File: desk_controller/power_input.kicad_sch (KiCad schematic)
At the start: 1 part

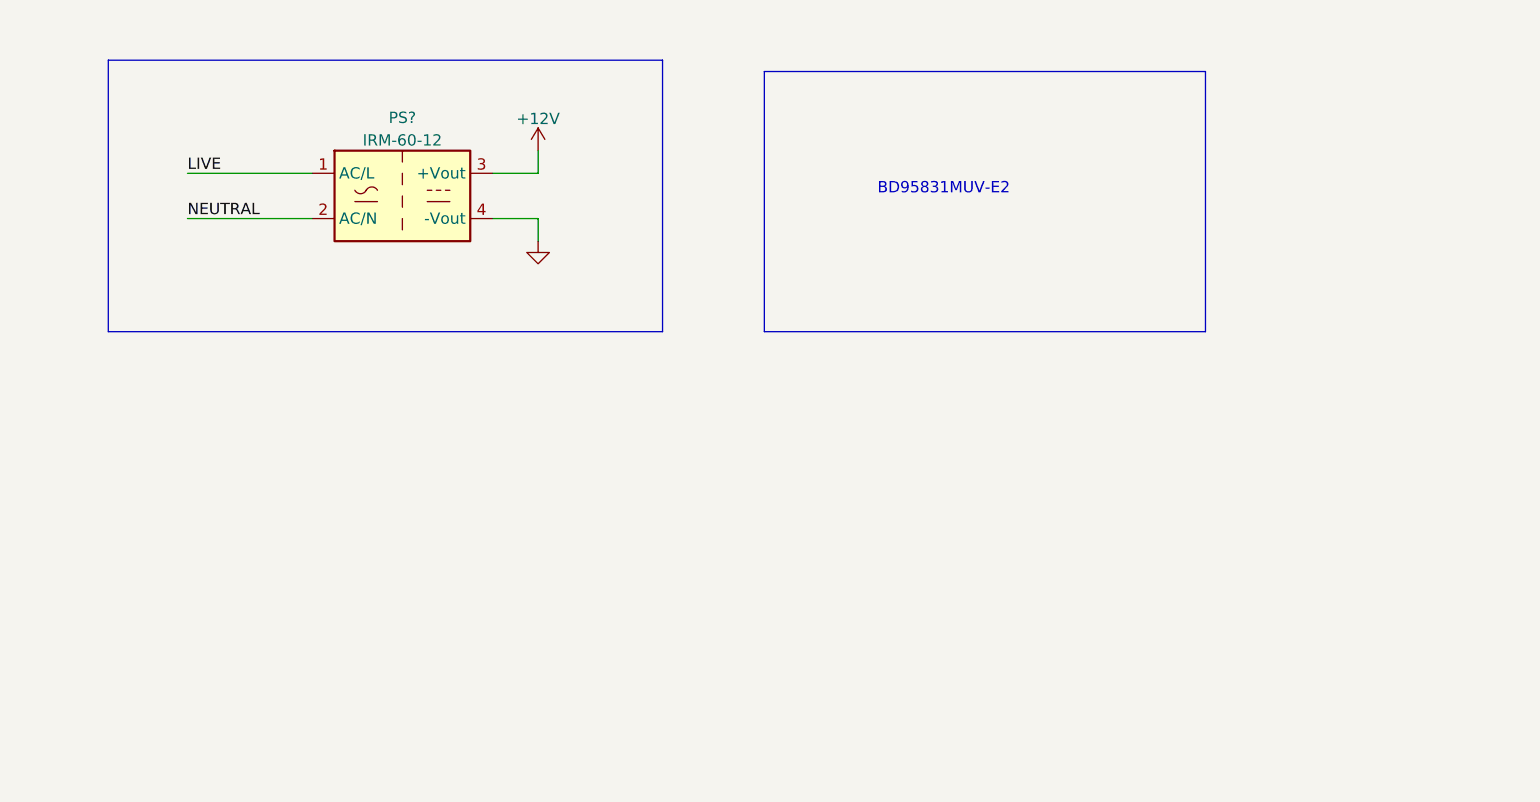
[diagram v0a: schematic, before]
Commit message: Buck converter sch, rs232 transceiver
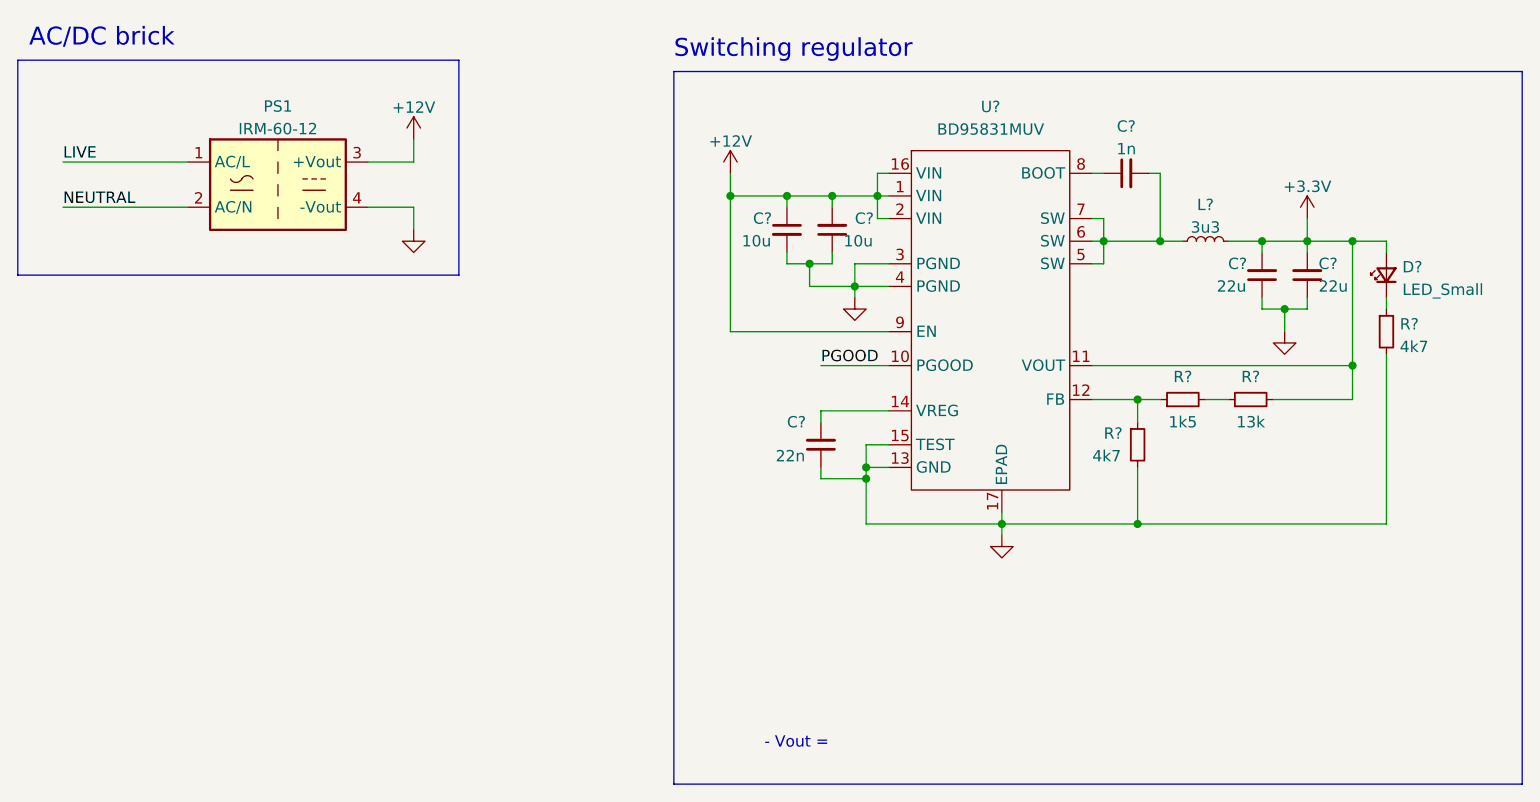
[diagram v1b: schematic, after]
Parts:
- added C? (x2): 22u, symbol Device:C_Small
- added C?: 22n, symbol Device:C_Small
- added C? (x2): 10u, symbol Device:C_Small
- added C?: 1n, symbol Device:C_Small
- added D?: LED_Small, symbol Device:LED_Small
- added L?: 3u3, symbol Device:L_Small
- added R? (x2): 4k7, symbol Device:R_Small
- added R?: 13k, symbol Device:R_Small
- added R?: 1k5, symbol Device:R_Small
- added U?: BD95831MUV, symbol BD95831MUV:BD95831MUV
- gave numbers to parts that had none: 1
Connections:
- net +12V: now also C?.1, C?.2, U?.1 (VIN), U?.16 (VIN), U?.2 (VIN), U?.9 (EN)
- net GND: now also C?.1, C?.1, C?.1, C?.1, C?.2, R?.2, R?.2, U?.13 (GND), U?.15 (TEST), U?.17 (EPAD), U?.3 (PGND), U?.4 (PGND)
- new net: R?.1, R?.1, U?.12 (FB)
- new net: C?.2, U?.14 (VREG)
- new net: C?.2, L?.1, U?.5 (SW), U?.6 (SW), U?.7 (SW)
- new net: C?.1, U?.8 (BOOT)
- new net: D?.1 (K), R?.1
- new net: R?.1, R?.2
- new net +3.3V: C?.2, C?.2, D?.2 (A), L?.2, R?.2, U?.11 (VOUT)
- new net PGOOD: U?.10 (PGOOD)
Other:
- note added: "- Vout ="
- note added: "AC/DC brick"
- note added: "Switching regulator"
- note removed: "BD95831MUV-E2"
- moved on the sheet: PS1

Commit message: Sch fixes, initial board layout
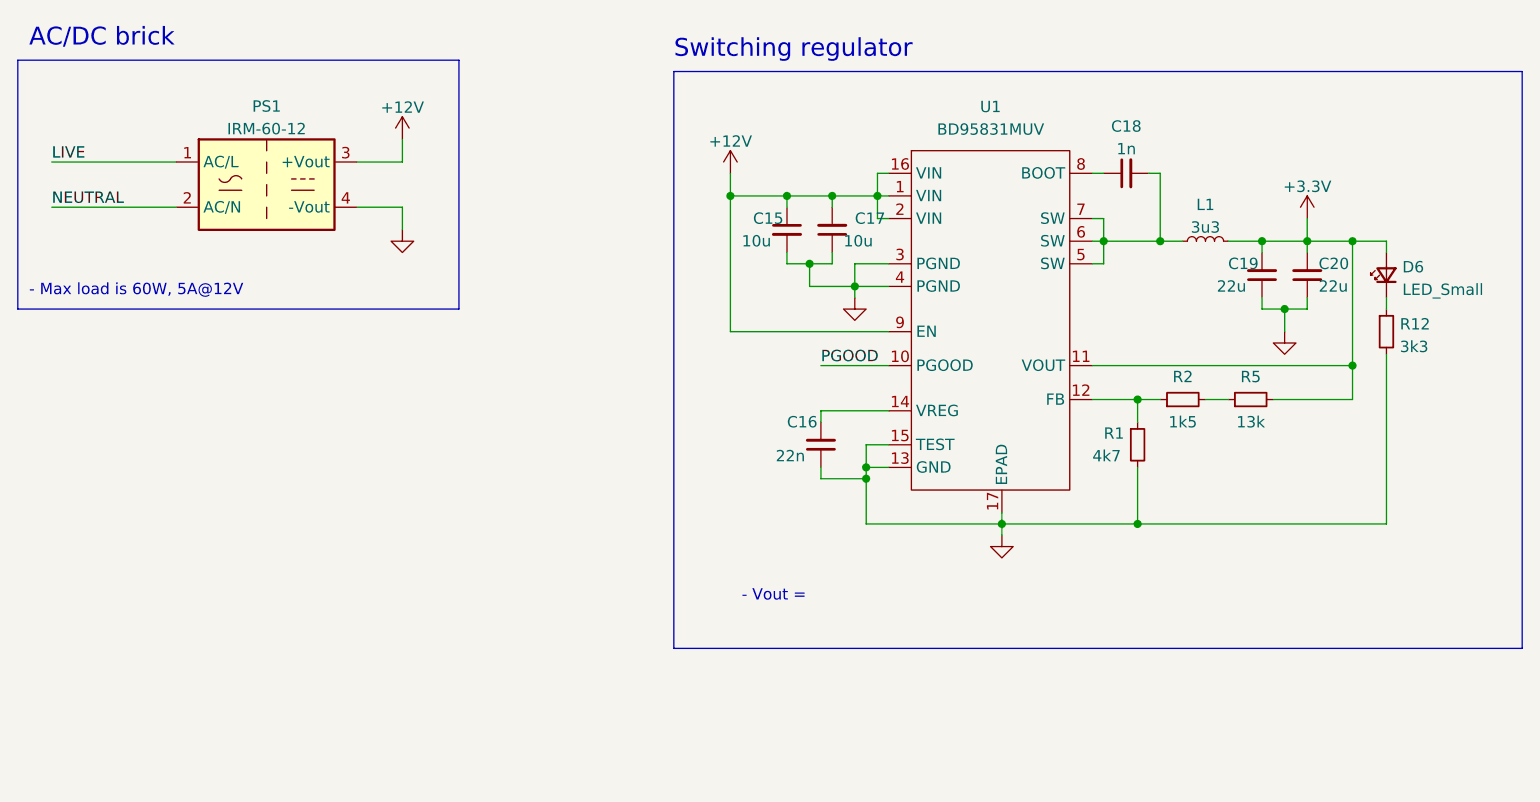
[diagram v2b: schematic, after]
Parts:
- C15, C16, C17, C18, C19, C20: renamed from C?; footprint (none) -> Capacitor_SMD:C_0603_1608Metric
- R1, R2, R5: renamed from R?; footprint (none) -> Resistor_SMD:R_0603_1608Metric
- R12: renamed from R?; value 4k7 -> 3k3; footprint (none) -> Resistor_SMD:R_0603_1608Metric
- U1: renamed from U?; footprint (none) -> Potentiometer_THT:Potentiometer_Bourns_3386F_Vertical
- gave numbers to parts that had none: 2
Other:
- note added: "- Max load is 60W, 5A@12V"
- moved on the sheet: PS1

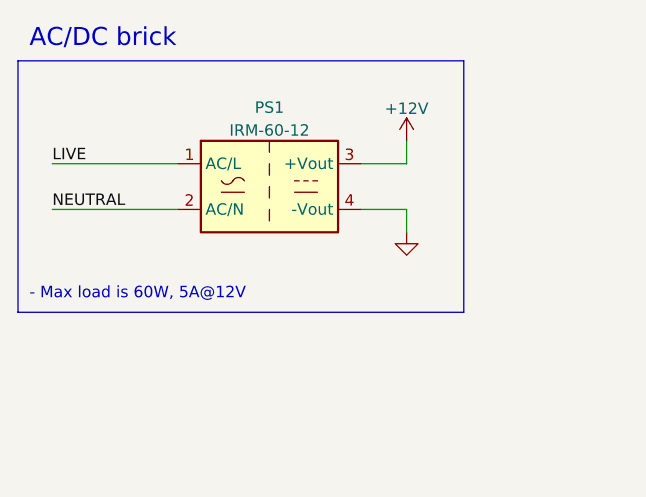
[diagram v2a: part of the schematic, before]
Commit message: Removed acdc brick
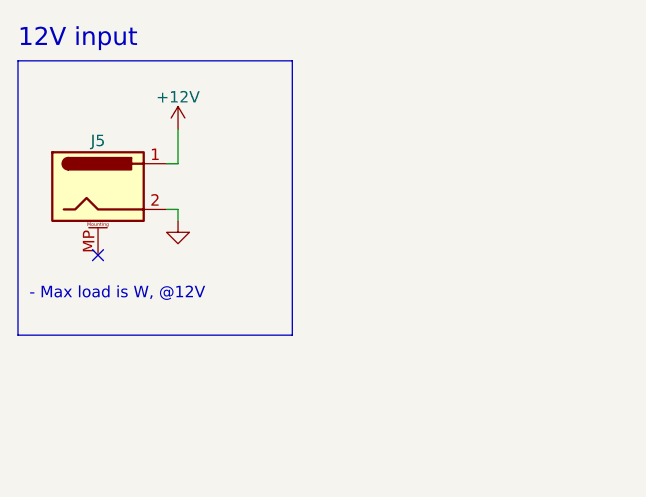
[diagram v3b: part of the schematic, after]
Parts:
- removed PS1: IRM-60-12, Converter_ACDC:Converter_ACDC_MeanWell_IRM-60-xx_THT, symbol Converter_ACDC:IRM-60-12
- added J5: Barrel_Jack_MountingPin, Connector_BarrelJack:BarrelJack_GCT_DCJ200-10-A_Horizontal, symbol Connector:Barrel_Jack_MountingPin
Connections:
- net +12V: now also J5.1
- net GND: now also J5.2
- no-connect marks 0 -> 1
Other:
- note added: "- Max load is W, @12V"
- note added: "12V input"
- note removed: "- Max load is 60W, 5A@12V"
- note removed: "AC/DC brick"
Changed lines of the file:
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@@
   (junction (at 162.56 68.58) (diameter 0) (color 0 0 0 0)
   )
+  (no_connect (at 74.93 74.93))
   (wire (pts (xy 201.93 73.66) (xy 205.74 73.66))
     (stroke (width 0) (type default) (color 0 0 0 0))
@@
     (stroke (width 0) (type default) (color 0 0 0 0))
   )
-  (polyline (pts (xy 66.04 53.34) (xy 115.57 53.34))
+  (polyline (pts (xy 66.04 53.34) (xy 96.52 53.34))
     (stroke (width 0) (type default) (color 0 0 0 0))
   )
@@
     (stroke (width 0) (type default) (color 0 0 0 0))
   )
+  (wire (pts (xy 83.82 60.96) (xy 83.82 64.77))
+    (stroke (width 0) (type default) (color 0 0 0 0))
+  )
   (wire (pts (xy 162.56 66.04) (xy 162.56 68.58))
     (stroke (width 0) (type default) (color 0 0 0 0))
@@
     (stroke (width 0) (type default) (color 0 0 0 0))
   )
-  (polyline (pts (xy 66.04 81.28) (xy 115.57 81.28))
-    (stroke (width 0) (type default) (color 0 0 0 0))
-  )
-  (wire (pts (xy 69.85 69.85) (xy 83.82 69.85))
+  (polyline (pts (xy 66.04 83.82) (xy 96.52 83.82))
     (stroke (width 0) (type default) (color 0 0 0 0))
   )
@@
     (stroke (width 0) (type default) (color 0 0 0 0))
   )
-  (wire (pts (xy 104.14 69.85) (xy 109.22 69.85))
-    (stroke (width 0) (type default) (color 0 0 0 0))
-  )
-  (wire (pts (xy 104.14 64.77) (xy 109.22 64.77))
-    (stroke (width 0) (type default) (color 0 0 0 0))
-  )
-  (polyline (pts (xy 66.04 53.34) (xy 66.04 81.28))
-    (stroke (width 0) (type default) (color 0 0 0 0))
-  )
-  (wire (pts (xy 69.85 64.77) (xy 83.82 64.77))
+  (polyline (pts (xy 66.04 53.34) (xy 66.04 83.82))
     (stroke (width 0) (type default) (color 0 0 0 0))
   )
@@
     (stroke (width 0) (type default) (color 0 0 0 0))
   )
+  (wire (pts (xy 83.82 69.85) (xy 83.82 71.12))
+    (stroke (width 0) (type default) (color 0 0 0 0))
+  )
   (wire (pts (xy 152.4 69.85) (xy 152.4 68.58))
     (stroke (width 0) (type default) (color 0 0 0 0))
@@
     (stroke (width 0) (type default) (color 0 0 0 0))
   )
-  (wire (pts (xy 109.22 62.23) (xy 109.22 64.77))
+  (wire (pts (xy 83.82 64.77) (xy 82.55 64.77))
     (stroke (width 0) (type default) (color 0 0 0 0))
   )
@@
     (stroke (width 0) (type default) (color 0 0 0 0))
   )
+  (wire (pts (xy 83.82 69.85) (xy 82.55 69.85))
+    (stroke (width 0) (type default) (color 0 0 0 0))
+  )
   (wire (pts (xy 163.83 83.82) (xy 146.05 83.82))
     (stroke (width 0) (type default) (color 0 0 0 0))
@@
     (stroke (width 0) (type default) (color 0 0 0 0))
   )
-  (polyline (pts (xy 115.57 81.28) (xy 115.57 53.34))
+  (polyline (pts (xy 96.52 83.82) (xy 96.52 53.34))
     (stroke (width 0) (type default) (color 0 0 0 0))
   )
@@
   )
   (wire (pts (xy 208.28 81.28) (xy 208.28 83.82))
-    (stroke (width 0) (type default) (color 0 0 0 0))
-  )
-  (wire (pts (xy 109.22 69.85) (xy 109.22 72.39))
     (stroke (width 0) (type default) (color 0 0 0 0))
   )
@@
     (effects (font (size 1.27 1.27)) (justify left bottom))
   )
-  (text "- Max load is 60W, 5A@12V" (at 67.31 80.01 0)
+  (text "- Max load is W, @12V" (at 67.31 80.01 0)
     (effects (font (size 1.27 1.27)) (justify left bottom))
   )
@@
     (effects (font (size 2 2)) (justify left bottom))
   )
-  (text "AC/DC brick" (at 67.31 52.07 0)
+  (text "12V input" (at 66.04 52.07 0)
     (effects (font (size 2 2)) (justify left bottom))
   )
-  (label "LIVE" (at 69.85 64.77 0)
-    (effects (font (size 1.27 1.27)) (justify left bottom))
-  )
   (label "PGOOD" (at 156.21 87.63 0)
-    (effects (font (size 1.27 1.27)) (justify left bottom))
-  )
-  (label "NEUTRAL" (at 69.85 69.85 0)
     (effects (font (size 1.27 1.27)) (justify left bottom))
   )
@@
     (pin "2")
   )
-  (symbol (lib_id "Converter_ACDC:IRM-60-12") (at 93.98 67.31 0) (unit 1)
-    (in_bom yes) (on_board yes) (fields_autoplaced)
-    (property "Reference" "PS1" (id 0) (at 93.98 58.5302 0))
-    (property "Value" "IRM-60-12" (id 1) (at 93.98 61.0671 0))
-    (property "Footprint" "Converter_ACDC:Converter_ACDC_MeanWell_IRM-60-xx_THT" (id 2) (at 93.98 77.47 0)
-      (effects (font (size 1.27 1.27)) hide)
-    )
-    (property "Datasheet" "http://www.meanwellusa.com/productPdf.aspx?i=687" (id 3) (at 93.98 67.31 0)
-      (effects (font (size 1.27 1.27)) hide)
-    )
-    (pin "1")
-    (pin "2")
-    (pin "3")
-    (pin "4")
-  )
   (symbol (lib_id "power:GND") (at 176.53 106.68 0) (unit 1)
     (in_bom yes) (on_board yes) (fields_autoplaced)
@@
     (pin "1")
   )
+  (symbol (lib_id "power:+12V") (at 83.82 60.96 0) (mirror y) (unit 1)
+    (in_bom yes) (on_board yes) (fields_autoplaced)
+    (property "Reference" "#PWR0111" (id 0) (at 83.82 64.77 0)
+      (effects (font (size 1.27 1.27)) hide)
+    )
+    (property "Value" "+12V" (id 1) (at 83.82 57.3842 0))
+    (property "Footprint" "" (id 2) (at 83.82 60.96 0)
+      (effects (font (size 1.27 1.27)) hide)
+    )
+    (property "Datasheet" "" (id 3) (at 83.82 60.96 0)
+      (effects (font (size 1.27 1.27)) hide)
+    )
+    (pin "1")
+  )
   (symbol (lib_id "Device:R_Small") (at 196.85 91.44 90) (unit 1)
     (in_bom yes) (on_board yes)
@@
     (pin "2")
   )
-  (symbol (lib_id "power:GND") (at 109.22 72.39 0) (unit 1)
-    (in_bom yes) (on_board yes) (fields_autoplaced)
-    (property "Reference" "#PWR0110" (id 0) (at 109.22 78.74 0)
-      (effects (font (size 1.27 1.27)) hide)
-    )
-    (property "Value" "GND" (id 1) (at 109.22 76.8334 0)
-      (effects (font (size 1.27 1.27)) hide)
-    )
-    (property "Footprint" "" (id 2) (at 109.22 72.39 0)
-      (effects (font (size 1.27 1.27)) hide)
-    )
-    (property "Datasheet" "" (id 3) (at 109.22 72.39 0)
-      (effects (font (size 1.27 1.27)) hide)
-    )
-    (pin "1")
-  )
-  (symbol (lib_id "power:+12V") (at 109.22 62.23 0) (unit 1)
-    (in_bom yes) (on_board yes) (fields_autoplaced)
-    (property "Reference" "#PWR0111" (id 0) (at 109.22 66.04 0)
-      (effects (font (size 1.27 1.27)) hide)
-    )
-    (property "Value" "+12V" (id 1) (at 109.22 58.6542 0))
-    (property "Footprint" "" (id 2) (at 109.22 62.23 0)
-      (effects (font (size 1.27 1.27)) hide)
-    )
-    (property "Datasheet" "" (id 3) (at 109.22 62.23 0)
-      (effects (font (size 1.27 1.27)) hide)
-    )
-    (pin "1")
+  (symbol (lib_id "power:GND") (at 83.82 71.12 0) (unit 1)
+    (in_bom yes) (on_board yes) (fields_autoplaced)
+    (property "Reference" "#PWR0110" (id 0) (at 83.82 77.47 0)
+      (effects (font (size 1.27 1.27)) hide)
+    )
+    (property "Value" "GND" (id 1) (at 83.82 75.5634 0)
+      (effects (font (size 1.27 1.27)) hide)
+    )
+    (property "Footprint" "" (id 2) (at 83.82 71.12 0)
+      (effects (font (size 1.27 1.27)) hide)
+    )
+    (property "Datasheet" "" (id 3) (at 83.82 71.12 0)
+      (effects (font (size 1.27 1.27)) hide)
+    )
+    (pin "1")
+  )
+  (symbol (lib_id "Connector:Barrel_Jack_MountingPin") (at 74.93 67.31 0) (unit 1)
+    (in_bom yes) (on_board yes)
+    (property "Reference" "J5" (id 0) (at 74.93 62.23 0))
+    (property "Value" "Barrel_Jack_MountingPin" (id 1) (at 74.93 62.3371 0)
+      (effects (font (size 1.27 1.27)) hide)
+    )
+    (property "Footprint" "Connector_BarrelJack:BarrelJack_GCT_DCJ200-10-A_Horizontal" (id 2) (at 76.2 68.326 0)
+      (effects (font (size 1.27 1.27)) hide)
+    )
+    (property "Datasheet" "~" (id 3) (at 76.2 68.326 0)
+      (effects (font (size 1.27 1.27)) hide)
+    )
+    (pin "1")
+    (pin "2")
+    (pin "MP")
   )
   (symbol (lib_id "Device:C_Small") (at 190.5 66.04 90) (unit 1)

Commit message: Much progress in sch and brd
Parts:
- removed C20: 22u, Capacitor_SMD:C_0603_1608Metric, symbol Device:C_Small
- removed D6: LED_Small, symbol Device:LED_Small
- removed L1: 3u3, symbol Device:L_Small
- removed R12: 3k3, Resistor_SMD:R_0603_1608Metric, symbol Device:R_Small
- removed U1: BD95831MUV, Potentiometer_THT:Potentiometer_Bourns_3386F_Vertical, symbol BD95831MUV:BD95831MUV
- added D6: RED, LED_SMD:LED_0603_1608Metric, symbol Device:LED
- added L1: 4u7, BWVS005050404R7M00:BWVS005050404R7M00, symbol Device:L
- added U1: TS30042-M000QFNR, Package_DFN_QFN:QFN-16-1EP_3x3mm_P0.5mm_EP1.75x1.75mm_ThermalVias, symbol TS30042:TS30042
- C15: rating (none) -> 50V
- C16: value 22n -> 100n; rating (none) -> 50V
- C17: value 10u -> 22n
- C18: value 1n -> 22u
- R1: value 4k7 -> 10k
- R2: value 1k5 -> 3k7
- R5: value 13k -> 1k
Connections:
- net +3.3V is gone; now on net +3V3: C19.2, R5.2
- net +12V: now also C15.2, C16.2, U1.11 (VCC), U1.2 (VCC), U1.3 (VCC); no longer C15.1, C17.2
- net GND: now also C15.1, C18.1, R2.2, D6.1 (K), U1.14 (PGND), U1.15 (PGND), U1.17 (PAD), U1.4 (GND); no longer C15.2, C17.1, R1.2
- net at R2.1: now also R1.2, U1.5 (FB); no longer R1.1
- net +3V3: now reaches C18.2
- net +3V3: now also R1.1, L1.2
- net at R5.1: now also D6.2 (A); no longer R2.2
- new net: C17.1, U1.10 (BST)
- new net: C17.2, L1.1, U1.1 (VSW), U1.12 (VSW), U1.13 (VSW), U1.16 (VSW)
- no-connect marks 1 -> 5
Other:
- note added: "-Vout = 0.9*(1 + Rtop/Rbottom), Rbottom should be 3750 -For the ADJ version, Vcc/Vout cannot exceed 16, 7.2727 in this case"
- note added: "3.3V regulator"
- note removed: "- Vout ="
- note removed: "Switching regulator"
- moved on the sheet: J5
